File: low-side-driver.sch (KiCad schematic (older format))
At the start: 4 parts, among them U2 74HC595

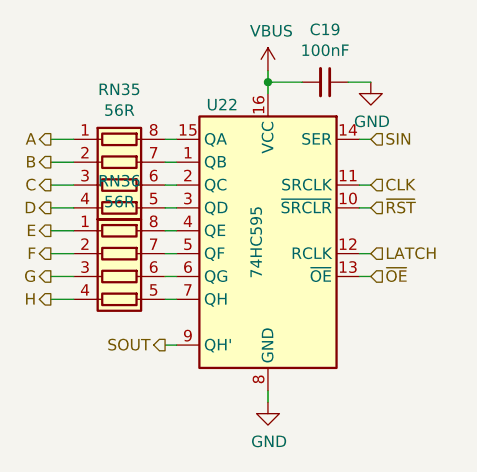
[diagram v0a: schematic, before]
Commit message: Finish STM32 digital interface assignment
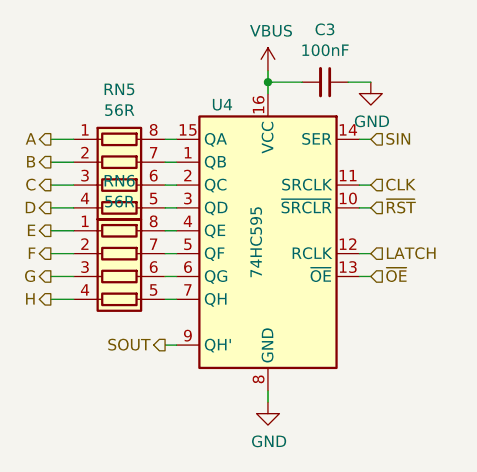
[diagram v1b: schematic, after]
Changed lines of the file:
@@
 $Descr A4 11693 8268
 encoding utf-8
-Sheet 15 24
+Sheet 5 25
 Title ""
 Date ""
@@
 AR Path="/61C4C905/61A75B6D/61A5FAFA" Ref="#PWR0153"  Part="1"
 AR Path="/61C4C905/61A75B93/61A5FAFA" Ref="#PWR0156"  Part="1"
-F 0 "#PWR0156" H 4900 3900 50  0001 C CNN
+F 0 "#PWR0107" H 4900 3900 50  0001 C CNN
 F 1 "GND" H 4905 3977 50  0000 C CNN
 F 2 "" H 4900 4150 50  0001 C CNN
@@
 AR Path="/61C4C905/61A75B6D/61A64A59" Ref="#PWR0154"  Part="1"
 AR Path="/61C4C905/61A75B93/61A64A59" Ref="#PWR0157"  Part="1"
-F 0 "#PWR0157" H 5350 2500 50  0001 C CNN
+F 0 "#PWR0108" H 5350 2500 50  0001 C CNN
 F 1 "GND" H 5355 2577 50  0000 C CNN
 F 2 "" H 5350 2750 50  0001 C CNN
@@
 AR Path="/61C4C905/61A75B6D/61A63F1A" Ref="C18"  Part="1"
 AR Path="/61C4C905/61A75B93/61A63F1A" Ref="C19"  Part="1"
-F 0 "C19" V 4921 2750 50  0000 C CNN
+F 0 "C3" V 4921 2750 50  0000 C CNN
 F 1 "100nF" V 5012 2750 50  0000 C CNN
 F 2 "Capacitor_SMD:C_0402_1005Metric" H 5150 2750 50  0001 C CNN
@@
 AR Path="/61C4C905/61A75B6D/61A5EC64" Ref="#PWR0155"  Part="1"
 AR Path="/61C4C905/61A75B93/61A5EC64" Ref="#PWR0158"  Part="1"
-F 0 "#PWR0158" H 4900 2550 50  0001 C CNN
+F 0 "#PWR0109" H 4900 2550 50  0001 C CNN
 F 1 "VBUS" H 4915 2873 50  0000 C CNN
 F 2 "" H 4900 2700 50  0001 C CNN
@@
 AR Path="/61C4C905/61A75B6D/61A5E6B7" Ref="RN34"  Part="1"
 AR Path="/61C4C905/61A75B93/61A5E6B7" Ref="RN36"  Part="1"
-F 0 "RN36" V 3833 3600 50  0000 C CNN
+F 0 "RN6" V 3833 3600 50  0000 C CNN
 F 1 "56R" V 3924 3600 50  0000 C CNN
 F 2 "Resistor_SMD:R_Array_Concave_4x0402" V 4525 3600 50  0001 C CNN
@@
 AR Path="/61C4C905/61A75B6D/61A5E6AC" Ref="RN33"  Part="1"
 AR Path="/61C4C905/61A75B93/61A5E6AC" Ref="RN35"  Part="1"
-F 0 "RN35" V 3833 3200 50  0000 C CNN
+F 0 "RN5" V 3833 3200 50  0000 C CNN
 F 1 "56R" V 3924 3200 50  0000 C CNN
 F 2 "Resistor_SMD:R_Array_Concave_4x0402" V 4525 3200 50  0001 C CNN
@@
 AR Path="/61C4C905/61A75B6D/61A5E6A5" Ref="U21"  Part="1"
 AR Path="/61C4C905/61A75B93/61A5E6A5" Ref="U22"  Part="1"
-F 0 "U22" H 5100 3950 50  0000 C CNN
+F 0 "U4" H 5100 3950 50  0000 C CNN
 F 1 "74HC595" V 4950 3350 50  0000 C CNN
 F 2 "Package_Texas:X1QFN-16-2.5x2.5-EP-1.2" H 4900 3400 50  0001 C CNN

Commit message: Add multiplexing MCU and USB
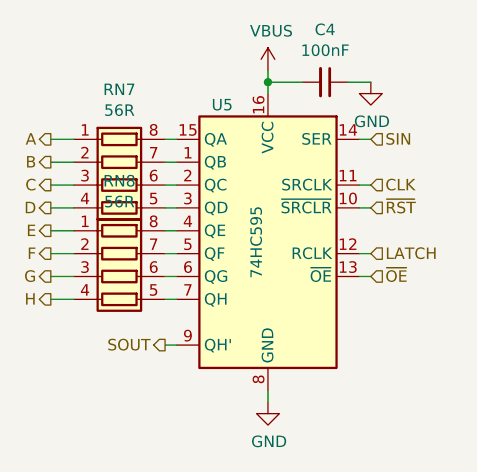
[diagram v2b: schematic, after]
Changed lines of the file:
@@
 $Descr A4 11693 8268
 encoding utf-8
-Sheet 5 25
+Sheet 6 25
 Title ""
 Date ""
@@
 AR Path="/61C4C905/61A75B6D/61A5FAFA" Ref="#PWR0153"  Part="1"
 AR Path="/61C4C905/61A75B93/61A5FAFA" Ref="#PWR0156"  Part="1"
-F 0 "#PWR0107" H 4900 3900 50  0001 C CNN
+F 0 "#PWR0110" H 4900 3900 50  0001 C CNN
 F 1 "GND" H 4905 3977 50  0000 C CNN
 F 2 "" H 4900 4150 50  0001 C CNN
@@
 AR Path="/61C4C905/61A75B6D/61A64A59" Ref="#PWR0154"  Part="1"
 AR Path="/61C4C905/61A75B93/61A64A59" Ref="#PWR0157"  Part="1"
-F 0 "#PWR0108" H 5350 2500 50  0001 C CNN
+F 0 "#PWR0111" H 5350 2500 50  0001 C CNN
 F 1 "GND" H 5355 2577 50  0000 C CNN
 F 2 "" H 5350 2750 50  0001 C CNN
@@
 AR Path="/61C4C905/61A75B6D/61A63F1A" Ref="C18"  Part="1"
 AR Path="/61C4C905/61A75B93/61A63F1A" Ref="C19"  Part="1"
-F 0 "C3" V 4921 2750 50  0000 C CNN
+F 0 "C4" V 4921 2750 50  0000 C CNN
 F 1 "100nF" V 5012 2750 50  0000 C CNN
 F 2 "Capacitor_SMD:C_0402_1005Metric" H 5150 2750 50  0001 C CNN
@@
 AR Path="/61C4C905/61A75B6D/61A5EC64" Ref="#PWR0155"  Part="1"
 AR Path="/61C4C905/61A75B93/61A5EC64" Ref="#PWR0158"  Part="1"
-F 0 "#PWR0109" H 4900 2550 50  0001 C CNN
+F 0 "#PWR0112" H 4900 2550 50  0001 C CNN
 F 1 "VBUS" H 4915 2873 50  0000 C CNN
 F 2 "" H 4900 2700 50  0001 C CNN
@@
 AR Path="/61C4C905/61A75B6D/61A5E6B7" Ref="RN34"  Part="1"
 AR Path="/61C4C905/61A75B93/61A5E6B7" Ref="RN36"  Part="1"
-F 0 "RN6" V 3833 3600 50  0000 C CNN
+F 0 "RN8" V 3833 3600 50  0000 C CNN
 F 1 "56R" V 3924 3600 50  0000 C CNN
 F 2 "Resistor_SMD:R_Array_Concave_4x0402" V 4525 3600 50  0001 C CNN
@@
 AR Path="/61C4C905/61A75B6D/61A5E6AC" Ref="RN33"  Part="1"
 AR Path="/61C4C905/61A75B93/61A5E6AC" Ref="RN35"  Part="1"
-F 0 "RN5" V 3833 3200 50  0000 C CNN
+F 0 "RN7" V 3833 3200 50  0000 C CNN
 F 1 "56R" V 3924 3200 50  0000 C CNN
 F 2 "Resistor_SMD:R_Array_Concave_4x0402" V 4525 3200 50  0001 C CNN
@@
 AR Path="/61C4C905/61A75B6D/61A5E6A5" Ref="U21"  Part="1"
 AR Path="/61C4C905/61A75B93/61A5E6A5" Ref="U22"  Part="1"
-F 0 "U4" H 5100 3950 50  0000 C CNN
+F 0 "U5" H 5100 3950 50  0000 C CNN
 F 1 "74HC595" V 4950 3350 50  0000 C CNN
 F 2 "Package_Texas:X1QFN-16-2.5x2.5-EP-1.2" H 4900 3400 50  0001 C CNN

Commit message: Add mounting pad for safety pin
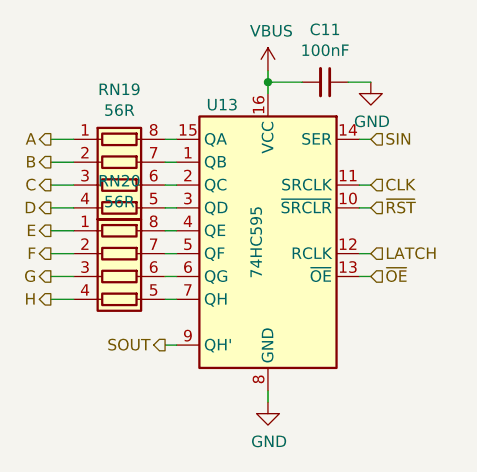
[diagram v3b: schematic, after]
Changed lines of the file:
@@
 $Descr A4 11693 8268
 encoding utf-8
-Sheet 6 25
+Sheet 14 25
 Title ""
 Date ""
@@
 AR Path="/61C4C905/61A75B6D/61A5FAFA" Ref="#PWR0153"  Part="1"
 AR Path="/61C4C905/61A75B93/61A5FAFA" Ref="#PWR0156"  Part="1"
-F 0 "#PWR0110" H 4900 3900 50  0001 C CNN
+F 0 "#PWR0132" H 4900 3900 50  0001 C CNN
 F 1 "GND" H 4905 3977 50  0000 C CNN
 F 2 "" H 4900 4150 50  0001 C CNN
@@
 AR Path="/61C4C905/61A75B6D/61A64A59" Ref="#PWR0154"  Part="1"
 AR Path="/61C4C905/61A75B93/61A64A59" Ref="#PWR0157"  Part="1"
-F 0 "#PWR0111" H 5350 2500 50  0001 C CNN
+F 0 "#PWR0133" H 5350 2500 50  0001 C CNN
 F 1 "GND" H 5355 2577 50  0000 C CNN
 F 2 "" H 5350 2750 50  0001 C CNN
@@
 AR Path="/61C4C905/61A75B6D/61A63F1A" Ref="C18"  Part="1"
 AR Path="/61C4C905/61A75B93/61A63F1A" Ref="C19"  Part="1"
-F 0 "C4" V 4921 2750 50  0000 C CNN
+F 0 "C11" V 4921 2750 50  0000 C CNN
 F 1 "100nF" V 5012 2750 50  0000 C CNN
 F 2 "Capacitor_SMD:C_0402_1005Metric" H 5150 2750 50  0001 C CNN
@@
 AR Path="/61C4C905/61A75B6D/61A5EC64" Ref="#PWR0155"  Part="1"
 AR Path="/61C4C905/61A75B93/61A5EC64" Ref="#PWR0158"  Part="1"
-F 0 "#PWR0112" H 4900 2550 50  0001 C CNN
+F 0 "#PWR0134" H 4900 2550 50  0001 C CNN
 F 1 "VBUS" H 4915 2873 50  0000 C CNN
 F 2 "" H 4900 2700 50  0001 C CNN
@@
 AR Path="/61C4C905/61A75B6D/61A5E6B7" Ref="RN34"  Part="1"
 AR Path="/61C4C905/61A75B93/61A5E6B7" Ref="RN36"  Part="1"
-F 0 "RN8" V 3833 3600 50  0000 C CNN
+F 0 "RN20" V 3833 3600 50  0000 C CNN
 F 1 "56R" V 3924 3600 50  0000 C CNN
 F 2 "Resistor_SMD:R_Array_Concave_4x0402" V 4525 3600 50  0001 C CNN
@@
 AR Path="/61C4C905/61A75B6D/61A5E6AC" Ref="RN33"  Part="1"
 AR Path="/61C4C905/61A75B93/61A5E6AC" Ref="RN35"  Part="1"
-F 0 "RN7" V 3833 3200 50  0000 C CNN
+F 0 "RN19" V 3833 3200 50  0000 C CNN
 F 1 "56R" V 3924 3200 50  0000 C CNN
 F 2 "Resistor_SMD:R_Array_Concave_4x0402" V 4525 3200 50  0001 C CNN
@@
 AR Path="/61C4C905/61A75B6D/61A5E6A5" Ref="U21"  Part="1"
 AR Path="/61C4C905/61A75B93/61A5E6A5" Ref="U22"  Part="1"
-F 0 "U5" H 5100 3950 50  0000 C CNN
+F 0 "U13" H 5100 3950 50  0000 C CNN
 F 1 "74HC595" V 4950 3350 50  0000 C CNN
 F 2 "Package_Texas:X1QFN-16-2.5x2.5-EP-1.2" H 4900 3400 50  0001 C CNN

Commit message: Make space for STM32
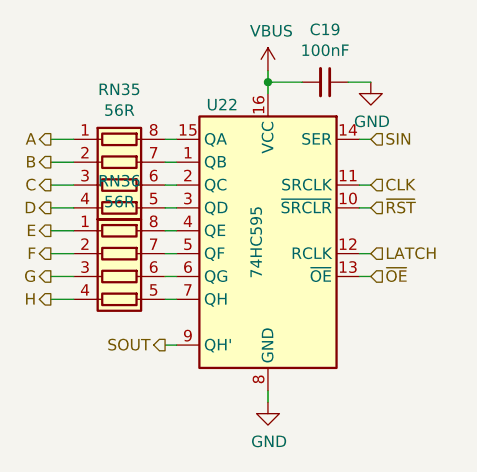
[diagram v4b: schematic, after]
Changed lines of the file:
@@
 $Descr A4 11693 8268
 encoding utf-8
-Sheet 14 25
+Sheet 23 25
 Title ""
 Date ""
@@
 AR Path="/61C4C905/61A75B6D/61A5FAFA" Ref="#PWR0153"  Part="1"
 AR Path="/61C4C905/61A75B93/61A5FAFA" Ref="#PWR0156"  Part="1"
-F 0 "#PWR0132" H 4900 3900 50  0001 C CNN
+F 0 "#PWR0156" H 4900 3900 50  0001 C CNN
 F 1 "GND" H 4905 3977 50  0000 C CNN
 F 2 "" H 4900 4150 50  0001 C CNN
@@
 AR Path="/61C4C905/61A75B6D/61A64A59" Ref="#PWR0154"  Part="1"
 AR Path="/61C4C905/61A75B93/61A64A59" Ref="#PWR0157"  Part="1"
-F 0 "#PWR0133" H 5350 2500 50  0001 C CNN
+F 0 "#PWR0157" H 5350 2500 50  0001 C CNN
 F 1 "GND" H 5355 2577 50  0000 C CNN
 F 2 "" H 5350 2750 50  0001 C CNN
@@
 AR Path="/61C4C905/61A75B6D/61A63F1A" Ref="C18"  Part="1"
 AR Path="/61C4C905/61A75B93/61A63F1A" Ref="C19"  Part="1"
-F 0 "C11" V 4921 2750 50  0000 C CNN
+F 0 "C19" V 4921 2750 50  0000 C CNN
 F 1 "100nF" V 5012 2750 50  0000 C CNN
 F 2 "Capacitor_SMD:C_0402_1005Metric" H 5150 2750 50  0001 C CNN
@@
 AR Path="/61C4C905/61A75B6D/61A5EC64" Ref="#PWR0155"  Part="1"
 AR Path="/61C4C905/61A75B93/61A5EC64" Ref="#PWR0158"  Part="1"
-F 0 "#PWR0134" H 4900 2550 50  0001 C CNN
+F 0 "#PWR0158" H 4900 2550 50  0001 C CNN
 F 1 "VBUS" H 4915 2873 50  0000 C CNN
 F 2 "" H 4900 2700 50  0001 C CNN
@@
 AR Path="/61C4C905/61A75B6D/61A5E6B7" Ref="RN34"  Part="1"
 AR Path="/61C4C905/61A75B93/61A5E6B7" Ref="RN36"  Part="1"
-F 0 "RN20" V 3833 3600 50  0000 C CNN
+F 0 "RN36" V 3833 3600 50  0000 C CNN
 F 1 "56R" V 3924 3600 50  0000 C CNN
 F 2 "Resistor_SMD:R_Array_Concave_4x0402" V 4525 3600 50  0001 C CNN
@@
 AR Path="/61C4C905/61A75B6D/61A5E6AC" Ref="RN33"  Part="1"
 AR Path="/61C4C905/61A75B93/61A5E6AC" Ref="RN35"  Part="1"
-F 0 "RN19" V 3833 3200 50  0000 C CNN
+F 0 "RN35" V 3833 3200 50  0000 C CNN
 F 1 "56R" V 3924 3200 50  0000 C CNN
 F 2 "Resistor_SMD:R_Array_Concave_4x0402" V 4525 3200 50  0001 C CNN
@@
 AR Path="/61C4C905/61A75B6D/61A5E6A5" Ref="U21"  Part="1"
 AR Path="/61C4C905/61A75B93/61A5E6A5" Ref="U22"  Part="1"
-F 0 "U13" H 5100 3950 50  0000 C CNN
+F 0 "U22" H 5100 3950 50  0000 C CNN
 F 1 "74HC595" V 4950 3350 50  0000 C CNN
 F 2 "Package_Texas:X1QFN-16-2.5x2.5-EP-1.2" H 4900 3400 50  0001 C CNN

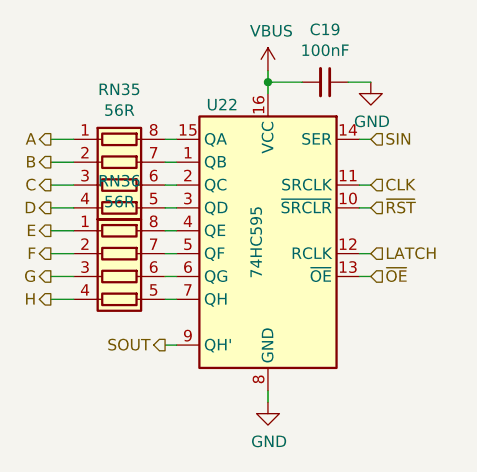
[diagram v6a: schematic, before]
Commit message: Add primary battery protection
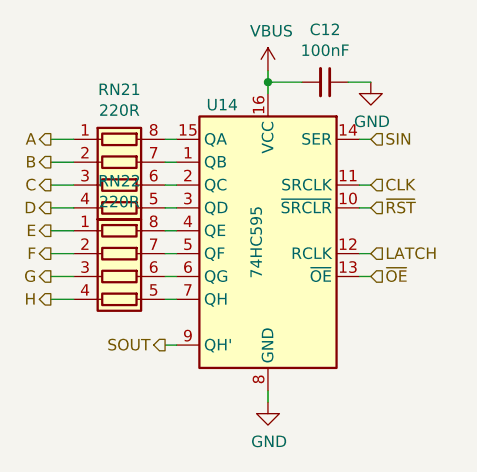
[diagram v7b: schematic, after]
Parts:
- RN1, RN2: value 56R -> 220R; LCSC C25504 -> C25498
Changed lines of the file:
@@
 $Descr A4 11693 8268
 encoding utf-8
-Sheet 11 25
+Sheet 15 25
 Title ""
 Date ""
@@
 AR Path="/61C4C905/61A75B6D/61A5FAFA" Ref="#PWR0153"  Part="1"
 AR Path="/61C4C905/61A75B93/61A5FAFA" Ref="#PWR0156"  Part="1"
-F 0 "#PWR0156" H 4900 3900 50  0001 C CNN
+F 0 "#PWR0135" H 4900 3900 50  0001 C CNN
 F 1 "GND" H 4905 3977 50  0000 C CNN
 F 2 "" H 4900 4150 50  0001 C CNN
@@
 AR Path="/61C4C905/61A75B6D/61A64A59" Ref="#PWR0154"  Part="1"
 AR Path="/61C4C905/61A75B93/61A64A59" Ref="#PWR0157"  Part="1"
-F 0 "#PWR0157" H 5350 2500 50  0001 C CNN
+F 0 "#PWR0136" H 5350 2500 50  0001 C CNN
 F 1 "GND" H 5355 2577 50  0000 C CNN
 F 2 "" H 5350 2750 50  0001 C CNN
@@
 AR Path="/61C4C905/61A75B6D/61A63F1A" Ref="C18"  Part="1"
 AR Path="/61C4C905/61A75B93/61A63F1A" Ref="C19"  Part="1"
-F 0 "C19" V 4921 2750 50  0000 C CNN
+F 0 "C12" V 4921 2750 50  0000 C CNN
 F 1 "100nF" V 5012 2750 50  0000 C CNN
 F 2 "Capacitor_SMD:C_0402_1005Metric" H 5150 2750 50  0001 C CNN
@@
 AR Path="/61C4C905/61A75B6D/61A5EC64" Ref="#PWR0155"  Part="1"
 AR Path="/61C4C905/61A75B93/61A5EC64" Ref="#PWR0158"  Part="1"
-F 0 "#PWR0158" H 4900 2550 50  0001 C CNN
+F 0 "#PWR0137" H 4900 2550 50  0001 C CNN
 F 1 "VBUS" H 4915 2873 50  0000 C CNN
 F 2 "" H 4900 2700 50  0001 C CNN
@@
 AR Path="/61C4C905/61A75B6D/61A5E6B7" Ref="RN34"  Part="1"
 AR Path="/61C4C905/61A75B93/61A5E6B7" Ref="RN36"  Part="1"
-F 0 "RN36" V 3833 3600 50  0000 C CNN
-F 1 "56R" V 3924 3600 50  0000 C CNN
+F 0 "RN22" V 3833 3600 50  0000 C CNN
+F 1 "220R" V 3924 3600 50  0000 C CNN
 F 2 "Resistor_SMD:R_Array_Concave_4x0402" V 4525 3600 50  0001 C CNN
 F 3 "~" H 4250 3600 50  0001 C CNN
-F 4 "C25504" V 4250 3600 50  0001 C CNN "LCSC"
+F 4 "C25498" V 4250 3600 50  0001 C CNN "LCSC"
 	1    4250 3600
 	0    1    1    0
@@
 AR Path="/61C4C905/61A75B6D/61A5E6AC" Ref="RN33"  Part="1"
 AR Path="/61C4C905/61A75B93/61A5E6AC" Ref="RN35"  Part="1"
-F 0 "RN35" V 3833 3200 50  0000 C CNN
-F 1 "56R" V 3924 3200 50  0000 C CNN
+F 0 "RN21" V 3833 3200 50  0000 C CNN
+F 1 "220R" V 3924 3200 50  0000 C CNN
 F 2 "Resistor_SMD:R_Array_Concave_4x0402" V 4525 3200 50  0001 C CNN
 F 3 "~" H 4250 3200 50  0001 C CNN
-F 4 "C25504" V 4250 3200 50  0001 C CNN "LCSC"
+F 4 "C25498" V 4250 3200 50  0001 C CNN "LCSC"
 	1    4250 3200
 	0    1    1    0
@@
 AR Path="/61C4C905/61A75B6D/61A5E6A5" Ref="U21"  Part="1"
 AR Path="/61C4C905/61A75B93/61A5E6A5" Ref="U22"  Part="1"
-F 0 "U22" H 5100 3950 50  0000 C CNN
+F 0 "U14" H 5100 3950 50  0000 C CNN
 F 1 "74HC595" V 4950 3350 50  0000 C CNN
 F 2 "Package_Texas:X1QFN-16-2.5x2.5-EP-1.2" H 4900 3400 50  0001 C CNN

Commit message: Finish layout
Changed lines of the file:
@@
 $Descr A4 11693 8268
 encoding utf-8
-Sheet 15 25
+Sheet 5 25
 Title ""
 Date ""
@@
 AR Path="/61C4C905/61A75B6D/61A5FAFA" Ref="#PWR0153"  Part="1"
 AR Path="/61C4C905/61A75B93/61A5FAFA" Ref="#PWR0156"  Part="1"
-F 0 "#PWR0135" H 4900 3900 50  0001 C CNN
+F 0 "#PWR0156" H 4900 3900 50  0001 C CNN
 F 1 "GND" H 4905 3977 50  0000 C CNN
 F 2 "" H 4900 4150 50  0001 C CNN
@@
 AR Path="/61C4C905/61A75B6D/61A64A59" Ref="#PWR0154"  Part="1"
 AR Path="/61C4C905/61A75B93/61A64A59" Ref="#PWR0157"  Part="1"
-F 0 "#PWR0136" H 5350 2500 50  0001 C CNN
+F 0 "#PWR0157" H 5350 2500 50  0001 C CNN
 F 1 "GND" H 5355 2577 50  0000 C CNN
 F 2 "" H 5350 2750 50  0001 C CNN
@@
 AR Path="/61C4C905/61A75B6D/61A63F1A" Ref="C18"  Part="1"
 AR Path="/61C4C905/61A75B93/61A63F1A" Ref="C19"  Part="1"
-F 0 "C12" V 4921 2750 50  0000 C CNN
+F 0 "C19" V 4921 2750 50  0000 C CNN
 F 1 "100nF" V 5012 2750 50  0000 C CNN
 F 2 "Capacitor_SMD:C_0402_1005Metric" H 5150 2750 50  0001 C CNN
@@
 AR Path="/61C4C905/61A75B6D/61A5EC64" Ref="#PWR0155"  Part="1"
 AR Path="/61C4C905/61A75B93/61A5EC64" Ref="#PWR0158"  Part="1"
-F 0 "#PWR0137" H 4900 2550 50  0001 C CNN
+F 0 "#PWR0158" H 4900 2550 50  0001 C CNN
 F 1 "VBUS" H 4915 2873 50  0000 C CNN
 F 2 "" H 4900 2700 50  0001 C CNN
@@
 AR Path="/61C4C905/61A75B6D/61A5E6B7" Ref="RN34"  Part="1"
 AR Path="/61C4C905/61A75B93/61A5E6B7" Ref="RN36"  Part="1"
-F 0 "RN22" V 3833 3600 50  0000 C CNN
+F 0 "RN36" V 3833 3600 50  0000 C CNN
 F 1 "220R" V 3924 3600 50  0000 C CNN
 F 2 "Resistor_SMD:R_Array_Concave_4x0402" V 4525 3600 50  0001 C CNN
@@
 AR Path="/61C4C905/61A75B6D/61A5E6AC" Ref="RN33"  Part="1"
 AR Path="/61C4C905/61A75B93/61A5E6AC" Ref="RN35"  Part="1"
-F 0 "RN21" V 3833 3200 50  0000 C CNN
+F 0 "RN35" V 3833 3200 50  0000 C CNN
 F 1 "220R" V 3924 3200 50  0000 C CNN
 F 2 "Resistor_SMD:R_Array_Concave_4x0402" V 4525 3200 50  0001 C CNN
@@
 AR Path="/61C4C905/61A75B6D/61A5E6A5" Ref="U21"  Part="1"
 AR Path="/61C4C905/61A75B93/61A5E6A5" Ref="U22"  Part="1"
-F 0 "U14" H 5100 3950 50  0000 C CNN
+F 0 "U22" H 5100 3950 50  0000 C CNN
 F 1 "74HC595" V 4950 3350 50  0000 C CNN
 F 2 "Package_Texas:X1QFN-16-2.5x2.5-EP-1.2" H 4900 3400 50  0001 C CNN
